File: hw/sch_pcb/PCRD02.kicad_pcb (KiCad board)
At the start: 2 copper layers, 50.3 x 30 mm, 40 parts, among them J1 CONN1_2, J2 JUMP_3X2, J3 JUMP_5X2, J4 Out, P1 _, P2 _, P3 _, P4 _, Q1 BF862, U1 AD8691, U2 AD8692

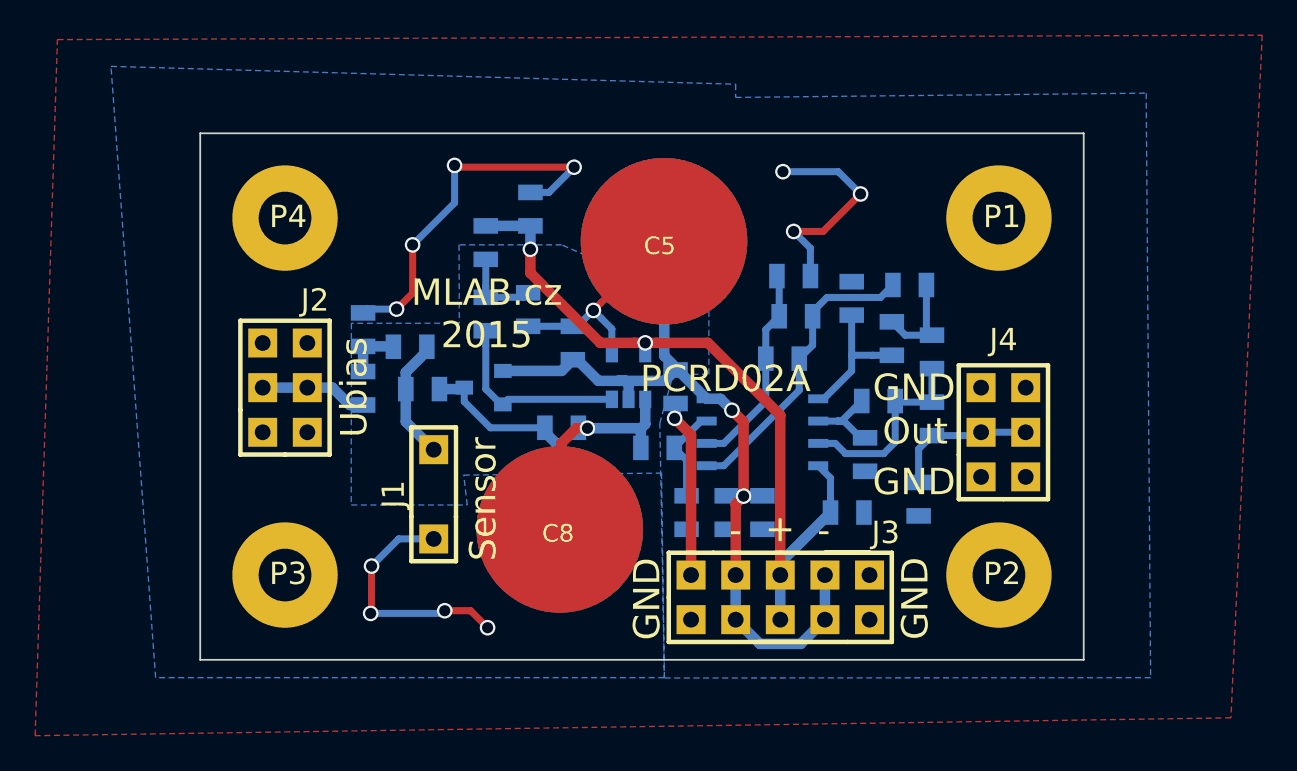
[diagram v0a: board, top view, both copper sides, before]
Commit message: Update project to KiCADv7, crop the title image.
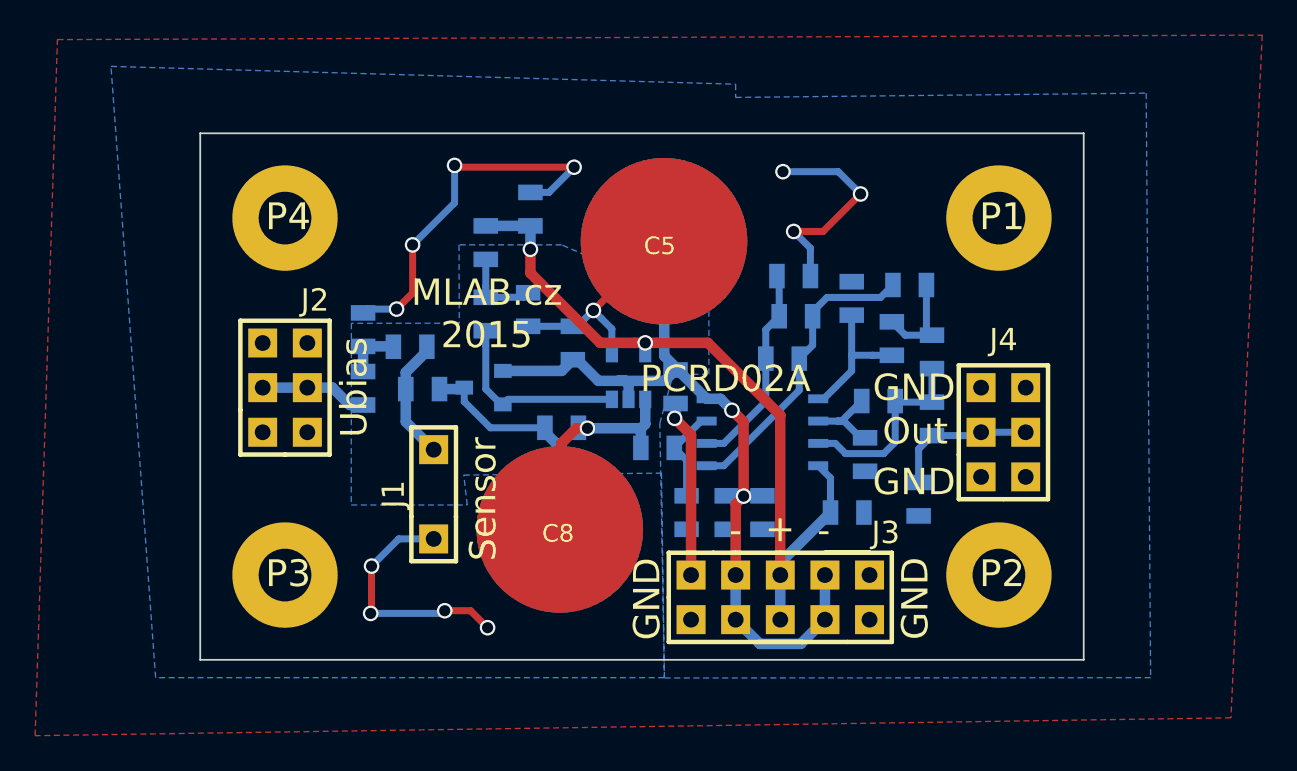
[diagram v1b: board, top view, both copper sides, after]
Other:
- net class Default removed
